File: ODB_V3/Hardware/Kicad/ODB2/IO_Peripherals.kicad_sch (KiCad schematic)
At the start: 33 parts, among them J1 142-0701-801, J10 MEM2067, J2 IdeFIX_GT17HN-4DP-2HA56, J3 RFD_GT17HN-4DP-2HA56, J4 USB_B_Micro, J5 SYS_SW_Conn_01x05_Header, J6 USBLC6-2P6, J7 Conn_02x04_Odd_Even, Q1 MMBT3904, U1 HM11, U2 L76L-M33, U9 W25Q512JVEIQ

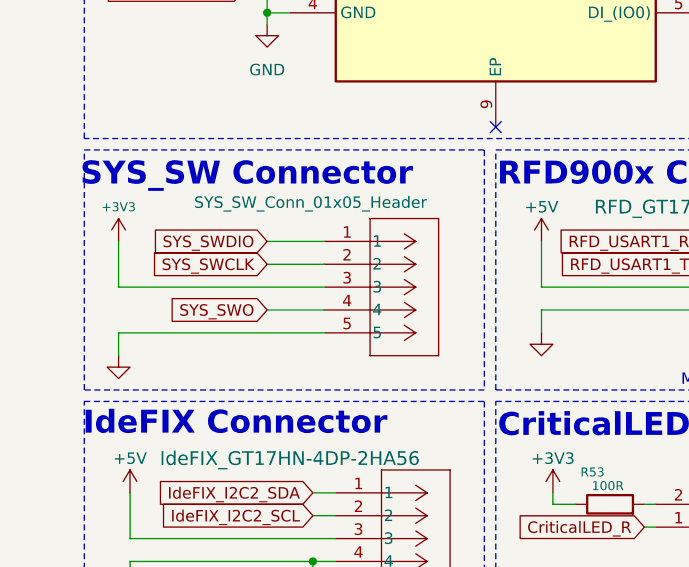
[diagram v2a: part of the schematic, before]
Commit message: wip: add nrst hardware stlink + change header 01x05->01x06
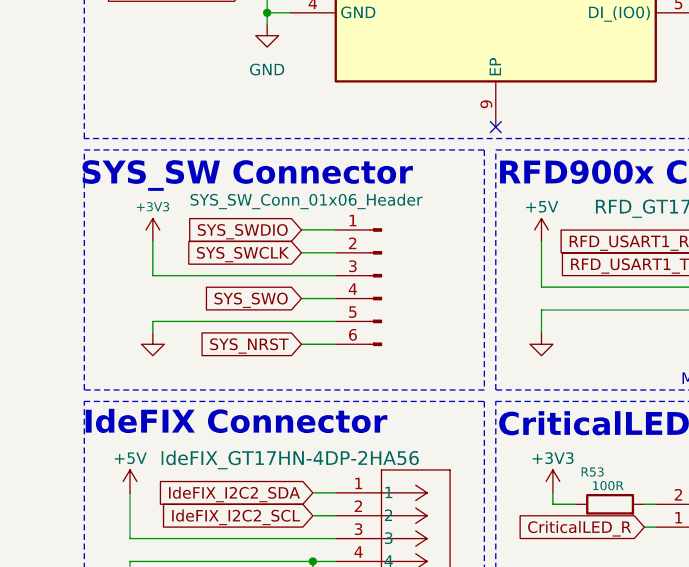
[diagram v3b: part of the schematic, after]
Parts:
- removed J5: SYS_SW_Conn_01x05_Header, Connector_PinHeader_2.54mm:PinHeader_1x05_P2.54mm_Vertical, symbol ODB2:705430004
- added J5: SYS_SW_Conn_01x06_Header, Connector_PinHeader_2.54mm:PinHeader_1x06_P2.54mm_Vertical, symbol Connector:Conn_01x06_Pin
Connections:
- net +3V3: now also J5.3 (Pin_3)
- net GND: now also J5.5 (Pin_5)
- net SYS_SWCLK: now also J5.2 (Pin_2)
- net SYS_SWDIO: now also J5.1 (Pin_1)
- net SYS_SWO: now also J5.4 (Pin_4)
- new net SYS_NRST: J5.6 (Pin_6)
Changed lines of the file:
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@@
 	(wire
 		(pts
-			(xy 34.29 68.58) (xy 40.64 68.58)
+			(xy 38.1 67.31) (xy 41.91 67.31)
+		)
+		(stroke
+			(width 0)
+			(type default)
+		)
+	)
+	(wire
+		(pts
+			(xy 21.59 72.39) (xy 41.91 72.39)
 		)
 		(stroke
@@
 	(wire
 		(pts
-			(xy 34.29 71.12) (xy 40.64 71.12)
+			(xy 38.1 69.85) (xy 41.91 69.85)
 		)
 		(stroke
@@
 	(wire
 		(pts
-			(xy 40.64 73.66) (xy 17.78 73.66)
-		)
-		(stroke
-			(width 0)
-			(type default)
-		)
-	)
-	(wire
-		(pts
 			(xy 39.37 99.06) (xy 41.91 99.06)
 		)
@@
 	(wire
 		(pts
-			(xy 17.78 78.74) (xy 17.78 81.28)
+			(xy 21.59 77.47) (xy 21.59 78.74)
 		)
 		(stroke
@@
 	(wire
 		(pts
+			(xy 21.59 77.47) (xy 41.91 77.47)
+		)
+		(stroke
+			(width 0)
+			(type default)
+		)
+	)
+	(wire
+		(pts
 			(xy 196.85 77.47) (xy 201.93 77.47)
 		)
@@
 	(wire
 		(pts
-			(xy 40.64 78.74) (xy 17.78 78.74)
-		)
-		(stroke
-			(width 0)
-			(type default)
-		)
-	)
-	(wire
-		(pts
 			(xy 223.52 35.56) (xy 223.52 36.83)
 		)
@@
 	(wire
 		(pts
-			(xy 17.78 73.66) (xy 17.78 68.58)
+			(xy 21.59 72.39) (xy 21.59 68.58)
 		)
 		(stroke
@@
 	(wire
 		(pts
-			(xy 34.29 76.2) (xy 40.64 76.2)
+			(xy 38.1 74.93) (xy 41.91 74.93)
 		)
 		(stroke
@@
 	(wire
 		(pts
+			(xy 38.1 80.01) (xy 41.91 80.01)
+		)
+		(stroke
+			(width 0)
+			(type default)
+		)
+	)
+	(wire
+		(pts
 			(xy 43.18 119.38) (xy 43.18 138.43)
 		)
@@
 	(global_label "SYS_SWDIO"
 		(shape input)
-		(at 34.29 68.58 180)
+		(at 38.1 67.31 180)
 		(fields_autoplaced yes)
 		(effects
@@
 		)
 		(property "Intersheetrefs" "${INTERSHEET_REFS}"
-			(at 20.9634 68.58 0)
+			(at 24.7734 67.31 0)
 			(effects
 				(font
@@
 	(global_label "SYS_SWCLK"
 		(shape input)
-		(at 34.29 71.12 180)
+		(at 38.1 69.85 180)
 		(fields_autoplaced yes)
 		(effects
@@
 		)
 		(property "Intersheetrefs" "${INTERSHEET_REFS}"
-			(at 20.6006 71.12 0)
+			(at 24.4106 69.85 0)
 			(effects
 				(font
@@
 	(global_label "SYS_SWO"
 		(shape input)
-		(at 34.29 76.2 180)
+		(at 38.1 74.93 180)
 		(fields_autoplaced yes)
 		(effects
@@
 		)
 		(property "Intersheetrefs" "${INTERSHEET_REFS}"
-			(at 22.8382 76.2 0)
+			(at 26.6482 74.93 0)
 			(effects
 				(font
@@
 		)
 	)
+	(global_label "SYS_NRST"
+		(shape input)
+		(at 38.1 80.01 180)
+		(fields_autoplaced yes)
+		(effects
+			(font
+				(size 1.27 1.27)
+				(thickness 0.1588)
+			)
+			(justify right)
+		)
+		(property "Intersheetrefs" "${INTERSHEET_REFS}"
+			(at 25.862 80.01 0)
+			(effects
+				(font
+					(size 1.27 1.27)
+				)
+				(justify right)
+				(hide yes)
+			)
+		)
+	)
 	(global_label "L76LM33_RF"
 		(shape input)
@@
 	(symbol
 		(lib_id "power:+3V3")
-		(at 17.78 68.58 0)
+		(at 21.59 68.58 0)
 		(unit 1)
 		(exclude_from_sim no)
@@
 		(dnp no)
 		(property "Reference" "#PWR046"
-			(at 17.78 72.39 0)
+			(at 21.59 72.39 0)
 			(effects
 				(font
@@
 		)
 		(property "Value" "+3V3"
-			(at 17.78 64.77 0)
+			(at 21.59 64.77 0)
 			(effects
 				(font
@@
 		)
 		(property "Footprint" ""
-			(at 17.78 68.58 0)
+			(at 21.59 68.58 0)
 			(effects
 				(font
@@
 		)
 		(property "Datasheet" ""
-			(at 17.78 68.58 0)
+			(at 21.59 68.58 0)
 			(effects
 				(font
@@
 		)
 		(property "Description" ""
-			(at 17.78 68.58 0)
+			(at 21.59 68.58 0)
 			(effects
 				(font
@@
 	(symbol
 		(lib_id "power:GND")
-		(at 17.78 81.28 0)
+		(at 21.59 78.74 0)
 		(unit 1)
 		(exclude_from_sim no)
@@
 		(fields_autoplaced yes)
 		(property "Reference" "#PWR047"
-			(at 17.78 87.63 0)
+			(at 21.59 85.09 0)
 			(effects
 				(font
@@
 		)
 		(property "Value" "GND"
-			(at 17.78 86.36 0)
+			(at 21.59 83.82 0)
 			(effects
 				(font
@@
 		)
 		(property "Footprint" ""
-			(at 17.78 81.28 0)
+			(at 21.59 78.74 0)
 			(effects
 				(font
@@
 		)
 		(property "Datasheet" ""
-			(at 17.78 81.28 0)
+			(at 21.59 78.74 0)
 			(effects
 				(font
@@
 		)
 		(property "Description" ""
-			(at 17.78 81.28 0)
+			(at 21.59 78.74 0)
 			(effects
 				(font
@@
 	)
 	(symbol
-		(lib_id "ODB2:705430004")
-		(at 40.64 68.58 0)
-		(unit 1)
-		(exclude_from_sim no)
-		(in_bom yes)
-		(on_board yes)
-		(dnp no)
-		(property "Reference" "J5"
-			(at 43.434 61.468 0)
-			(effects
-				(font
-					(size 1.524 1.524)
-				)
-				(justify left)
-				(hide yes)
-			)
-		)
-		(property "Value" "SYS_SW_Conn_01x05_Header"
-			(at 26.162 64.262 0)
-			(effects
-				(font
-					(size 1.27 1.27)
-				)
-				(justify left)
-			)
-		)
-		(property "Footprint" "Connector_PinHeader_2.54mm:PinHeader_1x05_P2.54mm_Vertical"
-			(at 30.734 61.976 0)
-			(effects
-				(font
-					(size 1.27 1.27)
-					(italic yes)
-				)
-				(hide yes)
-			)
-		)
-		(property "Datasheet" "705430004"
-			(at 59.436 65.024 0)
-			(effects
-				(font
-					(size 1.27 1.27)
-					(italic yes)
-				)
-				(hide yes)
-			)
-		)
-		(property "Description" ""
-			(at 40.64 68.58 0)
-			(effects
-				(font
-					(size 1.27 1.27)
-				)
-				(hide yes)
-			)
-		)
-		(property "DigiKey_Part_Number" ""
-			(at 40.64 68.58 0)
-			(effects
-				(font
-					(size 1.27 1.27)
-				)
-				(hide yes)
-			)
-		)
-		(property "Purchase-URL" ""
-			(at 40.64 68.58 0)
-			(effects
-				(font
-					(size 1.27 1.27)
-				)
-				(hide yes)
-			)
-		)
-		(property "Sim.Device" ""
-			(at 40.64 68.58 0)
-			(effects
-				(font
-					(size 1.27 1.27)
-				)
-				(hide yes)
-			)
-		)
-		(property "Sim.Pins" ""
-			(at 40.64 68.58 0)
-			(effects
-				(font
-					(size 1.27 1.27)
-				)
-				(hide yes)
-			)
-		)
-		(property "Sim.Type" ""
-			(at 40.64 68.58 0)
-			(effects
-				(font
-					(size 1.27 1.27)
-				)
-				(hide yes)
-			)
-		)
-		(pin "2"
-		)
-		(pin "4"
-		)
-		(pin "1"
-		)
-		(pin "5"
-		)
-		(pin "3"
-		)
-		(instances
-			(project ""
-				(path "/4b06c5d1-aa8b-48ed-8972-b43a60cfab78/93865dc8-71fa-4dc6-90ce-f5a9779dfd41"
-					(reference "J5")
-					(unit 1)
-				)
-			)
-		)
-	)
-	(symbol
 		(lib_id "ODB2:L76L-M33")
 		(at 109.22 151.13 0)
@@
 					(unit 1)
 				)
+			)
+		)
+	)
+	(symbol
+		(lib_id "Connector:Conn_01x06_Pin")
+		(at 46.99 72.39 0)
+		(mirror y)
+		(unit 1)
+		(exclude_from_sim no)
+		(in_bom yes)
+		(on_board yes)
+		(dnp no)
+		(property "Reference" "J5"
+			(at 46.355 62.23 0)
+			(effects
+				(font
+					(size 1.27 1.27)
+				)
+				(hide yes)
+			)
+		)
+		(property "Value" "SYS_SW_Conn_01x06_Header"
+			(at 38.608 64.008 0)
+			(effects
+				(font
+					(size 1.27 1.27)
+				)
+			)
+		)
+		(property "Footprint" "Connector_PinHeader_2.54mm:PinHeader_1x06_P2.54mm_Vertical"
+			(at 46.99 72.39 0)
+			(effects
+				(font
+					(size 1.27 1.27)
+				)
+				(hide yes)
+			)
+		)
+		(property "Datasheet" "~"
+			(at 46.99 72.39 0)
+			(effects
+				(font
+					(size 1.27 1.27)
+				)
+				(hide yes)
+			)
+		)
+		(property "Description" "Generic connector, single row, 01x06, script generated"
+			(at 46.99 72.39 0)
+			(effects
+				(font
+					(size 1.27 1.27)
+				)
+				(hide yes)
+			)
+		)
+		(pin "1"
+		)
+		(pin "2"
+		)
+		(pin "3"
+		)
+		(pin "4"
+		)
+		(pin "6"
+		)
+		(pin "5"
+		)
+		(instances
+			(project ""
+				(path "/4b06c5d1-aa8b-48ed-8972-b43a60cfab78/93865dc8-71fa-4dc6-90ce-f5a9779dfd41"
+					(reference "J5")
+					(unit 1)
+				)

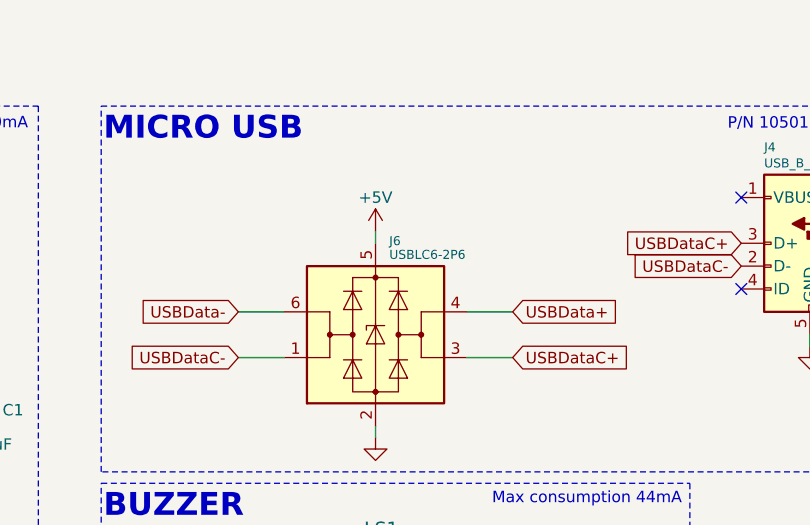
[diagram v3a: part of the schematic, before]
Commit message: feature : done all REFDES on silkscreen
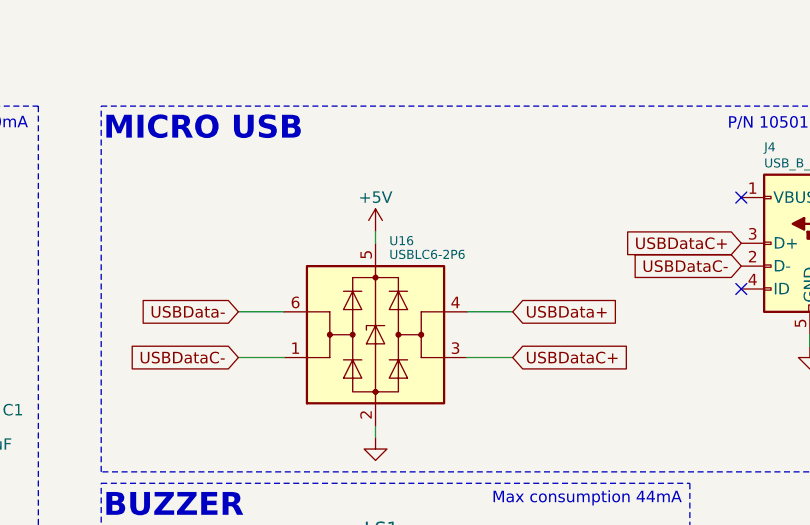
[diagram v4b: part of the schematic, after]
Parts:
- renumbered J6 to U16
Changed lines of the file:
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@@
 		(on_board yes)
 		(dnp no)
-		(property "Reference" "J6"
+		(property "Reference" "U16"
 			(at 225.044 36.576 0)
 			(effects
@@
 			(project "ODB2"
 				(path "/4b06c5d1-aa8b-48ed-8972-b43a60cfab78/93865dc8-71fa-4dc6-90ce-f5a9779dfd41"
-					(reference "J6")
+					(reference "U16")
 					(unit 1)
 				)

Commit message: wip : fill all components in BOM
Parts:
- C1: DigiKey_Part_Number (none) -> 490-13248-1-ND
- C2, C26, C37, C7: DigiKey_Part_Number (none) -> 311-3342-1-ND
- D1: DigiKey_Part_Number (none) -> 1516-QBLP601-AG15CT-ND
- R1, R11, R3: DigiKey_Part_Number (none) -> 408-1766-1-ND
- R16, R4: DigiKey_Part_Number (none) -> 311-10.0KHRCT-ND
- R2: DigiKey_Part_Number (none) -> 541-10.0LCT-ND
- R5, R53, R56: DigiKey_Part_Number (none) -> 764-1252-1-ND
- R50: DigiKey_Part_Number (none) -> 311-22.0LRCT-ND
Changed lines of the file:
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@@
 			)
 		)
-		(property "Datasheet" "~"
+		(property "Datasheet" "https://www.digikey.ca/en/products/detail/vishay-dale-thin-film/PCAN0603E1000BST5/6003299"
 			(at 115.57 100.33 0)
 			(effects
@@
 			)
 		)
-		(property "DigiKey_Part_Number" ""
+		(property "DigiKey_Part_Number" "764-1252-1-ND"
 			(at 115.57 100.33 90)
 			(effects
@@
 			)
 		)
-		(property "Datasheet" "~"
+		(property "Datasheet" "https://www.digikey.ca/en/products/detail/yageo/RC0603FR-0710KL/726880"
 			(at 171.45 48.26 0)
 			(effects
@@
 			)
 		)
-		(property "DigiKey_Part_Number" ""
+		(property "DigiKey_Part_Number" "311-10.0KHRCT-ND"
 			(at 171.45 48.26 90)
 			(effects
@@
 			)
 		)
-		(property "Datasheet" "~"
+		(property "Datasheet" "https://www.digikey.ca/en/products/detail/yageo/CC0402KRX5R9BB104/5883338"
 			(at 43.18 140.97 0)
 			(effects
@@
 			)
 		)
-		(property "DigiKey_Part_Number" ""
+		(property "DigiKey_Part_Number" "311-3342-1-ND"
 			(at 43.18 140.97 0)
 			(effects
@@
 			)
 		)
-		(property "Datasheet" "~"
+		(property "Datasheet" "https://www.digikey.ca/en/products/detail/susumu/URG1608L-152-L-T05/4552646"
 			(at 160.02 38.1 0)
 			(effects
@@
 			)
 		)
-		(property "DigiKey_Part_Number" ""
+		(property "DigiKey_Part_Number" "408-1766-1-ND"
 			(at 160.02 38.1 90)
 			(effects
@@
 			)
 		)
-		(property "Datasheet" "~"
+		(property "Datasheet" "https://www.digikey.ca/en/products/detail/vishay-dale-thin-film/PCAN0603E1000BST5/6003299"
 			(at 205.74 77.47 0)
 			(effects
@@
 			)
 		)
-		(property "DigiKey_Part_Number" ""
+		(property "DigiKey_Part_Number" "764-1252-1-ND"
 			(at 205.74 77.47 90)
 			(effects
@@
 			)
 		)
-		(property "Datasheet" "~"
+		(property "Datasheet" "https://www.digikey.ca/en/products/detail/yageo/CC0402KRX5R9BB104/5883338"
 			(at 48.26 30.48 0)
 			(effects
@@
 			)
 		)
-		(property "DigiKey_Part_Number" ""
+		(property "DigiKey_Part_Number" "311-3342-1-ND"
 			(at 48.26 30.48 90)
 			(effects
@@
 			)
 		)
-		(property "Datasheet" "~"
+		(property "Datasheet" "https://www.digikey.ca/en/products/detail/yageo/RC0402FR-0722RL/726562"
 			(at 38.1 121.92 0)
 			(effects
@@
 			)
 		)
-		(property "DigiKey_Part_Number" ""
+		(property "DigiKey_Part_Number" "311-22.0LRCT-ND"
 			(at 38.1 121.92 90)
 			(effects
@@
 			)
 		)
-		(property "Datasheet" "~"
+		(property "Datasheet" "https://www.digikey.ca/en/products/detail/yageo/RC0603FR-0710KL/726880"
 			(at 86.36 139.7 0)
 			(effects
@@
 			)
 		)
-		(property "DigiKey_Part_Number" ""
+		(property "DigiKey_Part_Number" "311-10.0KHRCT-ND"
 			(at 86.36 139.7 0)
 			(effects
@@
 			)
 		)
-		(property "Datasheet" "~"
+		(property "Datasheet" "https://www.digikey.ca/en/products/detail/vishay-dale/CRCW040210R0FKED/1177779"
 			(at 137.16 140.97 0)
 			(effects
@@
 			)
 		)
-		(property "DigiKey_Part_Number" ""
+		(property "DigiKey_Part_Number" "541-10.0LCT-ND"
 			(at 137.16 140.97 90)
 			(effects
@@
 			)
 		)
-		(property "Datasheet" "~"
+		(property "Datasheet" "https://www.digikey.ca/en/products/detail/qt-brightek-qtb/QBLP601-AG15/16499667"
 			(at 170.18 38.1 0)
 			(effects
@@
 			)
 		)
-		(property "DigiKey_Part_Number" ""
+		(property "DigiKey_Part_Number" "1516-QBLP601-AG15CT-ND"
 			(at 170.18 38.1 0)
 			(effects
@@
 			)
 		)
-		(property "Datasheet" "~"
+		(property "Datasheet" "https://www.digikey.ca/en/products/detail/susumu/URG1608L-152-L-T05/4552646"
 			(at 160.02 31.75 0)
 			(effects
@@
 			)
 		)
-		(property "DigiKey_Part_Number" ""
+		(property "DigiKey_Part_Number" "408-1766-1-ND"
 			(at 160.02 31.75 90)
 			(effects
@@
 			)
 		)
-		(property "Datasheet" "~"
+		(property "Datasheet" "https://www.digikey.ca/en/products/detail/susumu/URG1608L-152-L-T05/4552646"
 			(at 227.33 90.17 0)
 			(effects
@@
 			)
 		)
-		(property "DigiKey_Part_Number" ""
+		(property "DigiKey_Part_Number" "408-1766-1-ND"
 			(at 227.33 90.17 90)
 			(effects
@@
 			)
 		)
-		(property "Datasheet" "~"
+		(property "Datasheet" "https://www.digikey.ca/en/products/detail/yageo/CC0402KRX5R9BB104/5883338"
 			(at 165.1 57.15 0)
 			(effects
@@
 			)
 		)
-		(property "DigiKey_Part_Number" ""
+		(property "DigiKey_Part_Number" "311-3342-1-ND"
 			(at 165.1 57.15 0)
 			(effects
@@
 			)
 		)
-		(property "Datasheet" "~"
+		(property "Datasheet" "https://www.digikey.ca/en/products/detail/murata-electronics/GRM188R6YA106MA73D/5877411"
 			(at 177.8 57.15 0)
 			(effects
@@
 			)
 		)
-		(property "DigiKey_Part_Number" ""
+		(property "DigiKey_Part_Number" "490-13248-1-ND"
 			(at 177.8 57.15 0)
 			(effects
@@
 			)
 		)
-		(property "Datasheet" "~"
+		(property "Datasheet" "https://www.digikey.ca/en/products/detail/vishay-dale-thin-film/PCAN0603E1000BST5/6003299"
 			(at 72.39 97.79 0)
 			(effects
@@
 			)
 		)
-		(property "DigiKey_Part_Number" ""
+		(property "DigiKey_Part_Number" "764-1252-1-ND"
 			(at 72.39 97.79 90)
 			(effects
@@
 			)
 		)
-		(property "Datasheet" "~"
+		(property "Datasheet" "https://www.digikey.ca/en/products/detail/yageo/CC0402KRX5R9BB104/5883338"
 			(at 132.08 148.59 0)
 			(effects
@@
 			)
 		)
-		(property "DigiKey_Part_Number" ""
+		(property "DigiKey_Part_Number" "311-3342-1-ND"
 			(at 132.08 148.59 0)
 			(effects

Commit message: wip : done filling BOM, fix silkscreen, fix NRST hardware
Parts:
- D1: footprint LED_SMD:LED_0603_1608Metric -> ODB:LED_QBLP601-AG15
- J5: DigiKey_Part_Number (none) -> 732-5319-ND
- J7: DigiKey_Part_Number (none) -> 732-5296-ND
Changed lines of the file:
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@@
 			)
 		)
-		(property "Footprint" "LED_SMD:LED_0603_1608Metric"
+		(property "Footprint" "ODB:LED_QBLP601-AG15"
 			(at 170.18 38.1 0)
 			(effects
@@
 			)
 		)
-		(property "Datasheet" "~"
+		(property "Datasheet" "https://www.digikey.ca/en/products/detail/w%C3%BCrth-elektronik/61300611121/4846833"
 			(at 46.99 72.39 0)
 			(effects
@@
 		)
 		(property "Description" "Generic connector, single row, 01x06, script generated"
+			(at 46.99 72.39 0)
+			(effects
+				(font
+					(size 1.27 1.27)
+				)
+				(hide yes)
+			)
+		)
+		(property "DigiKey_Part_Number" "732-5319-ND"
 			(at 46.99 72.39 0)
 			(effects
@@
 			)
 		)
-		(property "Datasheet" "~"
+		(property "Datasheet" "https://www.digikey.ca/en/products/detail/w%C3%BCrth-elektronik/61300821121/4846841"
 			(at 247.65 149.86 0)
 			(effects
@@
 			)
 		)
-		(property "DigiKey_Part_Number" ""
+		(property "DigiKey_Part_Number" "732-5296-ND"
 			(at 247.65 149.86 0)
 			(effects

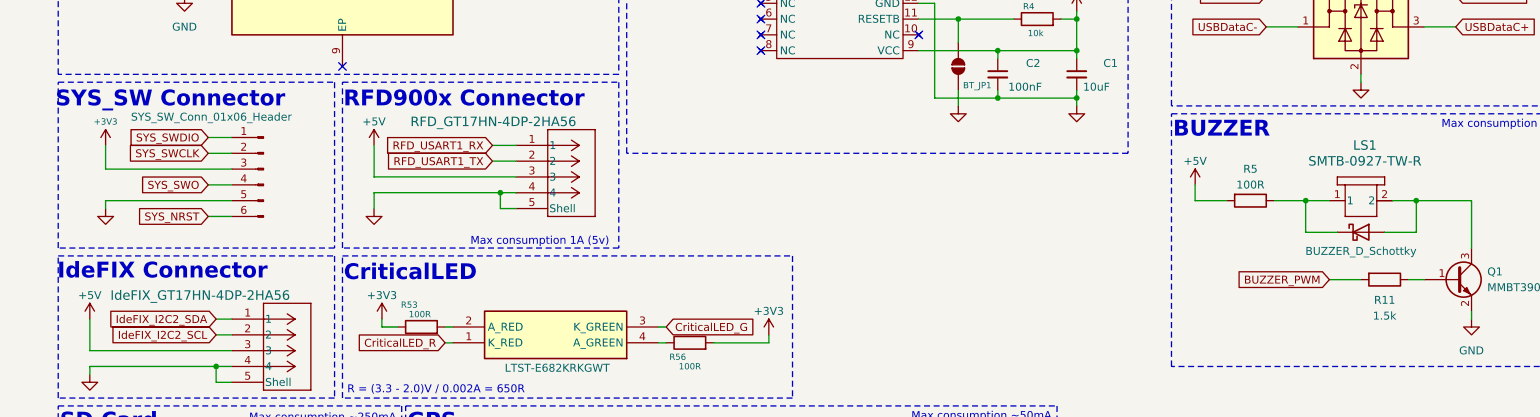
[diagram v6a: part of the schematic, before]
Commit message: wip : add MPN and fix footprints
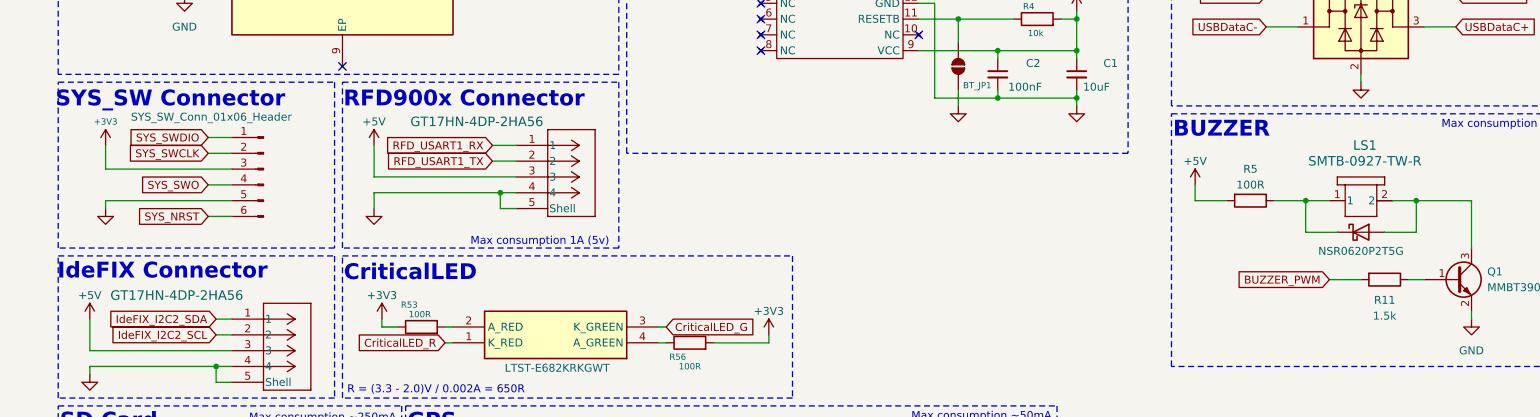
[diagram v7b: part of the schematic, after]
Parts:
- C1: Manufacturer_Part_Number (none) -> GRM188R6YA106MA73D
- C2, C26, C37, C7: Manufacturer_Part_Number (none) -> CC0402KRX5R9BB104
- D1: Manufacturer_Part_Number (none) -> QBLP601-AG15
- D2: value BUZZER_D_Schottky -> NSR0620P2T5G; footprint Diode_SMD:D_SOD-123 -> Diode_SMD:D_SOD-923; DigiKey_Part_Number BAT54T1GOSCT-ND -> NSR0620P2T5GOSCT-ND; Manufacturer_Part_Number (none) -> NSR0620P2T5G
- J1: Manufacturer_Part_Number (none) -> 142-0701-801
- J10: Manufacturer_Part_Number (none) -> MEM2067-02-180-00-A
- J2: value IdeFIX_GT17HN-4DP-2HA56 -> GT17HN-4DP-2HA56; Manufacturer_Part_Number (none) -> GT17HN-4DP-2H(A)(56)
- J3: value RFD_GT17HN-4DP-2HA56 -> GT17HN-4DP-2HA56; Manufacturer_Part_Number (none) -> GT17HN-4DP-2H(A)(56)
- J4: Manufacturer_Part_Number (none) -> 1050170001
- J5: Manufacturer_Part_Number (none) -> 61300611121
- J7: Manufacturer_Part_Number (none) -> 61300821121
- L1: DigiKey_Part_Number 541-ILSB0805ERR10KCT-ND -> 535-11609-1-ND; Manufacturer_Part_Number (none) -> AIML-0603-R10K-T
- LS1: Manufacturer_Part_Number (none) -> SMTB-0927-TW-R
- Q1: Manufacturer_Part_Number (none) -> MMBT3904LT1G
- R1, R11, R3: Manufacturer_Part_Number (none) -> URG1608L-152-L-T05
- R16, R4: Manufacturer_Part_Number (none) -> RC0603FR-0710KL
- R2: Manufacturer_Part_Number (none) -> CRCW040210R0FKED
- R5, R53, R56: Manufacturer_Part_Number (none) -> PCAN0603E1000BST5
- R50: Manufacturer_Part_Number (none) -> RC0402FR-0722RL
- U16: Manufacturer_Part_Number (none) -> USBLC6-2P6
- U2: Manufacturer_Part_Number (none) -> L76L-M33
